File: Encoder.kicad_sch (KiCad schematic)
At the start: 12 parts, among them J4 DE9_Socket, U3 AM26LS32ACDR, U4 AP2151AW-7

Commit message: wip
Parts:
- J4: footprint Connector_Dsub:DSUB-9_Pins_EdgeMount_P2.77mm -> Connector_Dsub:DSUB-9_Socket_Vertical_P2.77x2.84mm_MountingHoles
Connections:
- net +3.3V: now also R17.2; no longer C13.2, R16.1, U3.16 (VCC)
- net +5V: no longer R17.2
- net 5V_Encoder: now also C13.2, R16.1, U3.16 (VCC)
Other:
- note added: "Either R15 or R16 is fitted Or one is connected to GPIO for EN"
- note added: "Need of logic shift 5V -> 3.3V"
- note removed: "Either R15 or R16 is fitted"
- moved on the sheet: C13, R12, R13, R14, R15, R16, R17, U3

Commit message: wip
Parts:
- added U2: AP3012, Package_TO_SOT_SMD:SOT-23-5, symbol Regulator_Switching:AP3012
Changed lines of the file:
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@@
 	)
 	(image
-		(at 107.95 -41.91)
+		(at 106.68 -26.67)
 		(scale 0.533682)
 		(data "iVBORw0KGgoAAAANSUhEUgAABM8AAAFYCAYAAABETNuSAAAAAXNSR0IArs4c6QAAAARnQU1BAACx"
@@
 					(unit 1)
 				)
+			)
+		)
+	)
+	(symbol
+		(lib_id "Regulator_Switching:AP3012")
+		(at 172.72 59.69 0)
+		(mirror y)
+		(unit 1)
+		(exclude_from_sim no)
+		(in_bom yes)
+		(on_board yes)
+		(dnp no)
+		(property "Reference" "U2"
+			(at 172.72 50.8 0)
+			(effects
+				(font
+					(size 1.27 1.27)
+				)
+			)
+		)
+		(property "Value" "AP3012"
+			(at 172.72 53.34 0)
+			(effects
+				(font
+					(size 1.27 1.27)
+				)
+			)
+		)
+		(property "Footprint" "Package_TO_SOT_SMD:SOT-23-5"
+			(at 172.085 66.04 0)
+			(effects
+				(font
+					(size 1.27 1.27)
+					(italic yes)
+				)
+				(justify left)
+				(hide yes)
+			)
+		)
+		(property "Datasheet" "https://www.diodes.com/assets/Datasheets/AP3012.pdf"
+			(at 172.72 59.69 0)
+			(effects
+				(font
+					(size 1.27 1.27)
+				)
+				(hide yes)
+			)
+		)
+		(property "Description" "500mA, Adjustable Step-Up Voltage Regulator, 1.5MHz Frequency, SOT-23-5"
+			(at 172.72 59.69 0)
+			(effects
+				(font
+					(size 1.27 1.27)
+				)
+				(hide yes)
+			)
+		)
+		(pin "1"
+		)
+		(pin "4"
+		)
+		(pin "2"
+		)
+		(pin "5"
+		)
+		(pin "3"
+		)
+		(instances
+			(project ""
+				(path "/d122ff09-cd02-4f53-acb5-49b9ee3003a4/a853fa18-1554-4543-86ef-20ec948ab35c"
+					(reference "U2")
+					(unit 1)
+				)

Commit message: wip
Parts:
- removed U2: AP3012, Package_TO_SOT_SMD:SOT-23-5, symbol Regulator_Switching:AP3012
- added Q1, Q2, Q3: BSS138, Package_TO_SOT_SMD:SOT-23, symbol Transistor_FET:BSS138
- added R11, R19, R20, R21, R22, R23: 10k, Resistor_SMD:R_0805_2012Metric, symbol Device:R
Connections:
- net +3.3V: now also Q1.1 (G), Q2.1 (G), Q3.1 (G), R19.2, R21.2, R23.2
- net +5V: now also R11.1, R20.1, R22.1
- net Encoder_0: now also Q3.2 (S), R23.1; no longer U3.13 (4Y)
- net Encoder_A: now also Q1.2 (S), R19.1; no longer U3.3 (1Y)
- net Encoder_B: now also Q2.2 (S), R21.1; no longer U3.5 (2Y)
- new net: Q1.3 (D), R11.2, U3.3 (1Y)
- new net: Q3.3 (D), R22.2, U3.13 (4Y)
- new net: Q2.3 (D), R20.2, U3.5 (2Y)
- no-connect marks 2 -> 3
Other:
- note added: "ESD?"
- note added: "RS-422 DE9 plug"
- note added: "RS422 to digital Encoder interface"
- note added: "Short Circuit Protection"
- note removed: "Need of logic shift 5V -> 3.3V"
- moved on the sheet: C13, C14, J4, R12, R13, R14, R15, R16, R17, R18, U3, U4

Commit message: 90% schematic first layout
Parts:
- removed Q1, Q2, Q3: BSS138, Package_TO_SOT_SMD:SOT-23, symbol Transistor_FET:BSS138
- removed R19, R20, R21, R22, R23: 10k, Resistor_SMD:R_0805_2012Metric, symbol Device:R
- added C21, C22: 100n, Capacitor_SMD:C_0805_2012Metric_Pad1.18x1.45mm_HandSolder, symbol Device:C
- added U8: 4504, Package_SO:SOIC-16_3.9x9.9mm_P1.27mm, symbol 4xxx:4504
- J4: footprint Connector_Dsub:DSUB-9_Socket_Vertical_P2.77x2.84mm_MountingHoles -> Connector_Dsub:DSUB-9_Pins_Horizontal_P2.77x2.84mm_EdgePinOffset4.94mm_Housed_MountingHolesOffset4.94mm
- R15, R16: value 1k -> 10k
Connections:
- net +3.3V: now also C22.1, U8.16 (VDD)
- net +5V: no longer R11.1
- net 5V_Encoder: now also R11.1, C21.2, U8.1 (VCC)
- net Encoder_0: now also U8.6 (Cout)
- net Encoder_A: now also U8.2 (Aout)
- net Encoder_B: now also U8.4 (Bout)
- net GNDD: now also C21.1, C22.2, U8.11 (Ein), U8.14 (Fin), U8.8 (VSS), U8.9 (Din)
- net at U3.3 (1Y): now also U8.3 (Ain); no longer R11.2
- net at U3.13 (4Y): now also U8.7 (Cin)
- net at U3.5 (2Y): now also U8.5 (Bin)
- new net: R11.2, U8.13 (Select)
- no-connect marks 3 -> 6
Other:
- moved on the sheet: C13

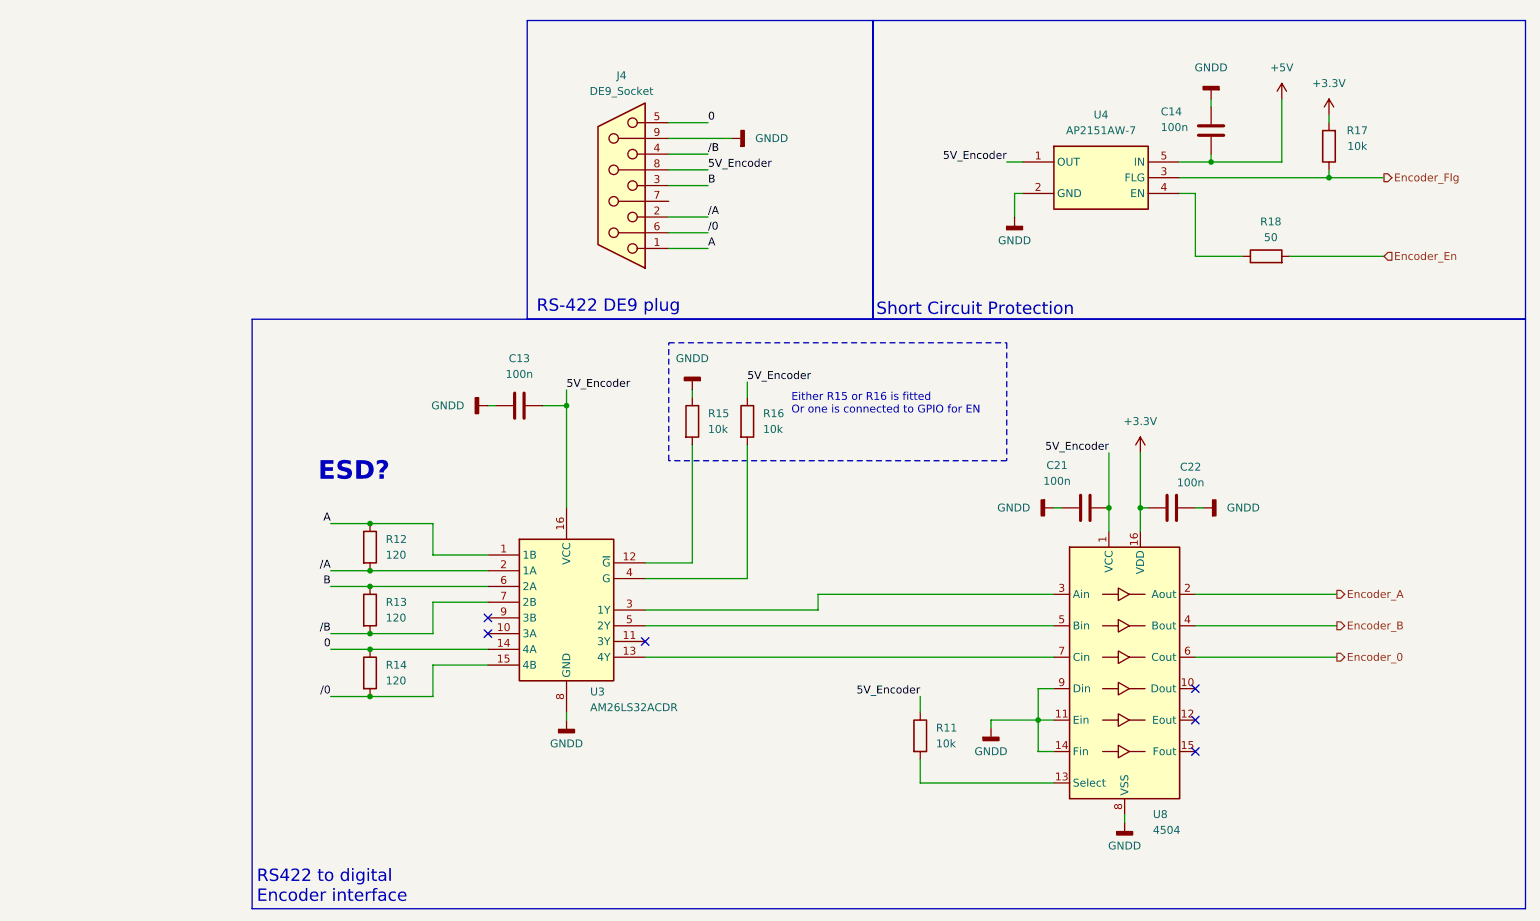
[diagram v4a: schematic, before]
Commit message: Addition of testpoints
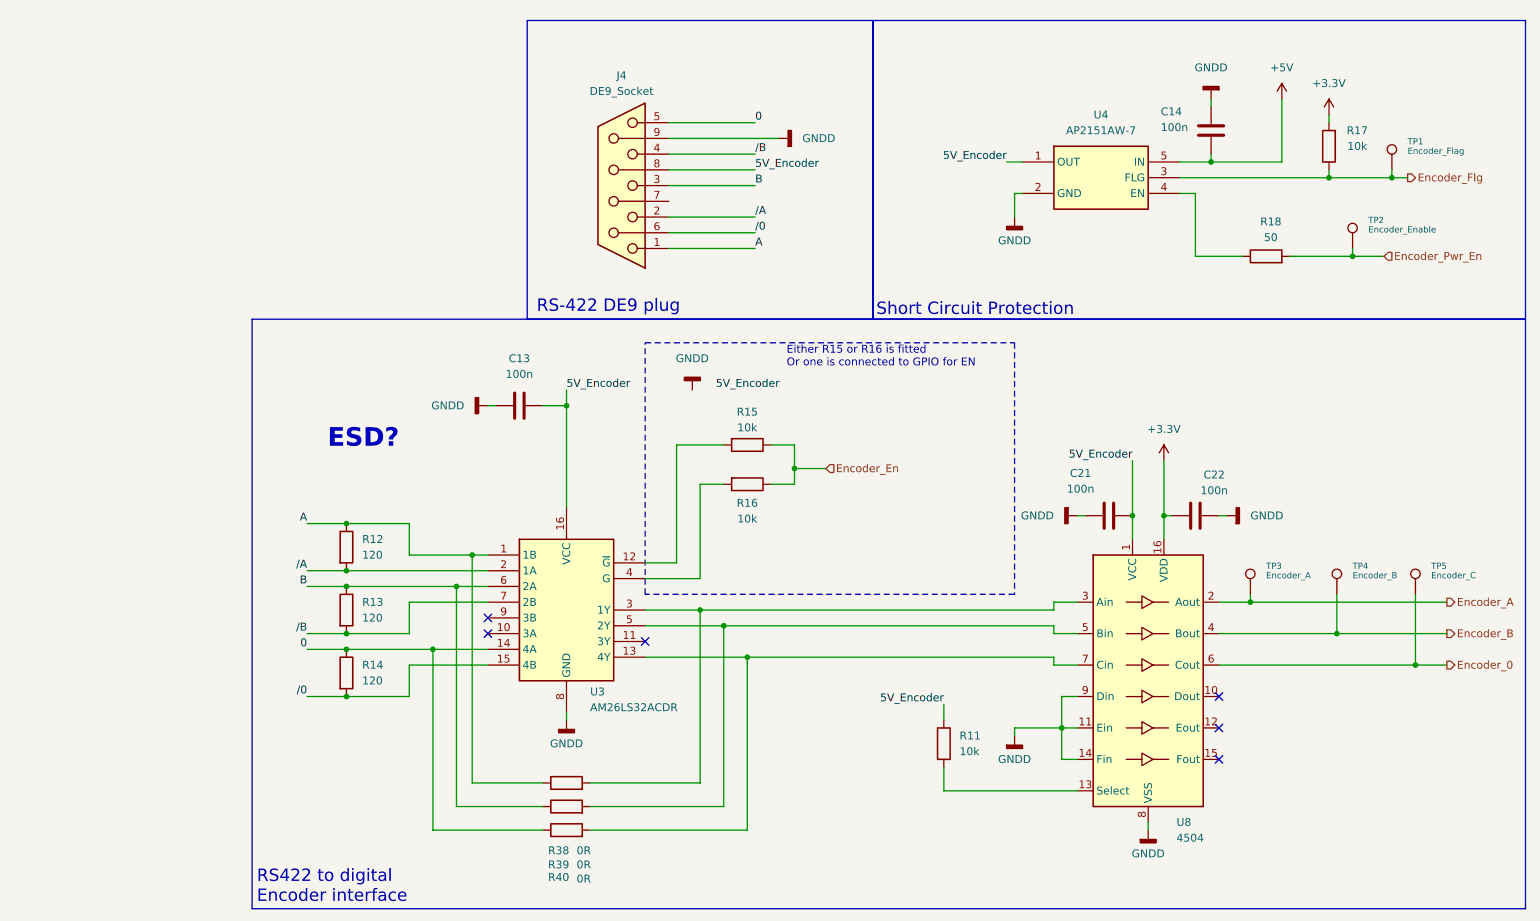
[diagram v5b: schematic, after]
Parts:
- added R38, R39, R40: 0R, Resistor_SMD:R_0805_2012Metric, symbol Device:R
- added TP1: Encoder_Flag, TestPoint:TestPoint_Pad_D1.0mm, symbol Connector:TestPoint
- added TP2: Encoder_Enable, TestPoint:TestPoint_Pad_D1.0mm, symbol Connector:TestPoint
- added TP3: Encoder_A, TestPoint:TestPoint_Pad_D1.0mm, symbol Connector:TestPoint
- added TP4: Encoder_B, TestPoint:TestPoint_Pad_D1.0mm, symbol Connector:TestPoint
- added TP5: Encoder_C, TestPoint:TestPoint_Pad_D1.0mm, symbol Connector:TestPoint
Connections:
- net 0: now also R40.1
- net 5V_Encoder: no longer R16.1
- net A: now also R38.1
- net B: now also R39.1
- net Encoder_0: now also TP5.1
- net Encoder_A: now also TP3.1
- net Encoder_B: now also TP4.1
- net Encoder_En: now also R15.1, R16.1; no longer R18.2
- net Encoder_Flg: now also TP1.1
- net GNDD: no longer R15.1
- net at U3.13 (4Y), U8.7 (Cin): now also R40.2
- net at U3.3 (1Y), U8.3 (Ain): now also R38.2
- net at U3.5 (2Y), U8.5 (Bin): now also R39.2
- new net Encoder_Pwr_En: R18.2, TP2.1
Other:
- moved on the sheet: C21, C22, R11, R12, R13, R14, R15, R16, U8
